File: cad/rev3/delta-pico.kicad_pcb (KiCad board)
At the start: 2 copper layers, 77.7 x 166.3 mm, 84 parts, among them J1 Conn_01x02, J2 Conn_01x14, J3 Conn_01x08, J4 Conn_01x04, J5 Conn_01x02, Q1 2N7002K, SW1 SW_SPDT, SW10 SW_Push, SW11 SW_Push, SW12 SW_Push, SW13 SW_Push, SW14 SW_Push, SW15 SW_Push, SW16 SW_Push, SW17 SW_Push, SW18 SW_Push, SW19 SW_Push, SW2 SW_Push, SW20 SW_Push, SW21 SW_Push, SW22 SW_Push, SW23 SW_Push, SW24 SW_Push, SW25 SW_Push, SW26 SW_Push, SW27 SW_Push, SW28 SW_Push, SW29 SW_Push, SW3 SW_Push, SW30 SW_Push, SW31 SW_Push, SW4 SW_Push, SW5 SW_Push, SW6 SW_Push, SW7 SW_Push, SW8 SW_Push, SW9 SW_Push, U1 PCF8574A, U2 PCF8574A, U3 Pico, U4 24LC16

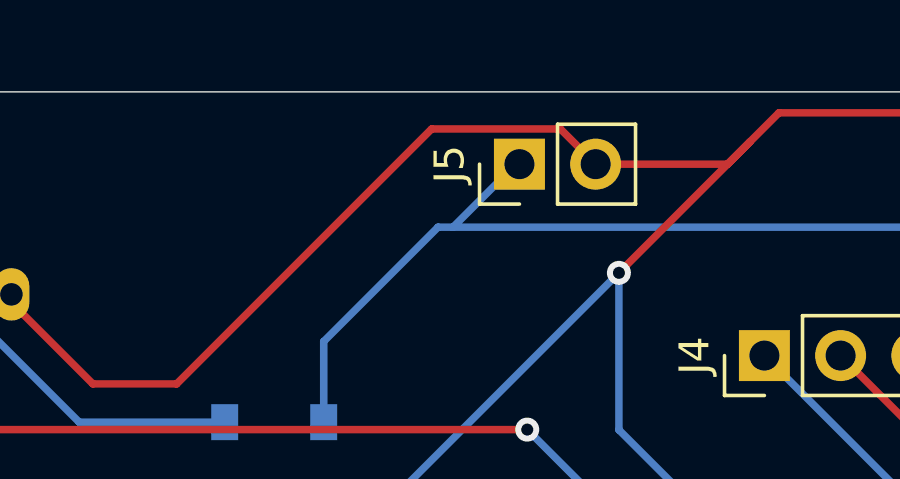
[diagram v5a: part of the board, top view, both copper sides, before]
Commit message: Remove stray silkscreen
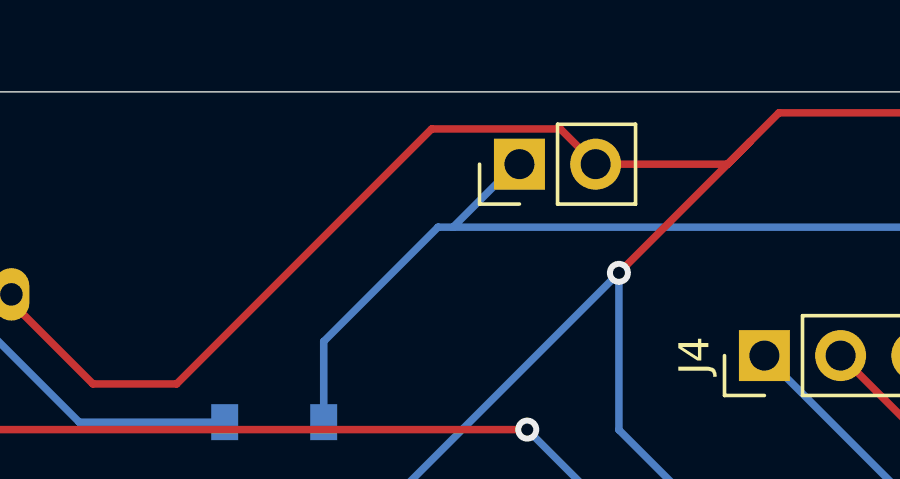
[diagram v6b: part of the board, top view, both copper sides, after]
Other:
- board text added: "VSYS"
- board text removed: "BYP. VSYS"
- board text removed: "SW. VSYS"
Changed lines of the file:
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@@
     (property "Sheetname" "")
     (attr through_hole)
-    (fp_text reference "J5" (at 0 -2.33 90) (layer "F.SilkS")
+    (fp_text reference "J5" (at 0 -2.33 90) (layer "F.SilkS") hide
       (effects (font (size 1 1) (thickness 0.15)))
     )
@@
     (effects (font (size 1 1) (thickness 0.15)) (justify mirror))
   )
-  (gr_text "BYP. VSYS" (at 59.65 28.53 90) (layer "B.SilkS")
+  (gr_text "VSYS" (at 59.69 26.924 90) (layer "B.SilkS")
     (effects (font (size 0.8 0.8) (thickness 0.15)) (justify mirror))
   )
-  (gr_text "SW. VSYS" (at 56.98 28.23 90) (layer "B.SilkS")
-    (effects (font (size 0.8 0.8) (thickness 0.15)) (justify mirror))
-  )
